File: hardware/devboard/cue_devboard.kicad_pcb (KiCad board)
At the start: 4 copper layers, 42 x 32 mm, 56 parts, among them J1 USB-C (power), J2 BATT, J3 LRA, J4 SWD, J5 EXP, SW1 USER, SW2 SHIP/WAKE, U1 BL54L15, U2 nPM1300, U3 LSM6DSV16BX, U4 T5838, U5 DRV2605L

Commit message: Dev board: fixes from the second layout review
- battery polarity marked (+/-) at J2; README: meter the cell's plug first
- LRA connector moved so the motor lines stay 2 mm from PDM_CLK, 5 mm from the mic hole
- nPM1300 exposed pad: 4 vias in the gaps between paste openings (no solder wicking)
- vias moved off the RT1, C6, C8 pads (via_off_pads.py); L1 joins C6 on top copper
- U3 pin 7 tied to ground (C8 shifted 0.4 mm, QVAR1 re-routed)
- silkscreen at JLCPCB minimums (1.0 mm text), TP net labels, button labels on top
- SW1/SW2 left out of BOM/CPL (hand-solder); fab/placement_check.png for the JLCPCB preview
DRC 0 violations, 0 unconnected; board = circuit pad for pad.

Co-Authored-By: Claude Opus 5.5 <noreply@anthropic.com>
Claude-Session: https://claude.ai/code/session_01DUSU7jbUyc6QVB5XjyAbxC
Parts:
- moved J3 12.0 mm to (35.0, 28.8)
- moved E1 8.00 mm to (23.0, 29.0)
- moved SW1 3.72 mm to (28.0, 24.2)
- moved C8 0.40 mm to (23.6, 20.7)
- turned C6 to -90 degrees
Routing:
- net VBAT: track 67.9 -> 86.3 mm, vias 3 -> 5
- net CC1: track 30.2 -> 16.2 mm
- net MIC_1V8: track 54.4 -> 42.8 mm
- net PDM_CLK: track 29.8 -> 19.6 mm
- net LRA_P: track 21.8 -> 29.2 mm, vias 2 -> 0
- net PMIC_INT: track 32.1 -> 37.6 mm, vias 3 -> 1
- net TDM_WCLK: track 13.9 -> 18.6 mm
- net 3V0: track 44.1 -> 39.7 mm, vias 2 -> 3
- net VSYS: track 57.6 -> 62.0 mm
- net TOUCH_E: track 11.1 -> 7.22 mm
- net I2C_SCL: track 63.8 -> 67.1 mm, vias 3 -> 4
- net HAPTIC_EN: track 11.7 -> 9.08 mm
- net MIC_WAKE: track 8.53 -> 10.9 mm, vias 0 -> 2
- net GND: track 48.5 -> 46.3 mm, vias 164 -> 159
- net MIC_THSEL: track 17.3 -> 15.3 mm
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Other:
- board text added: "+"
- board text added: "-"
- board text added: "1V8"
- board text added: "3V0"
- board text added: "BATT"
- board text added: "GND"
- board text added: "I2C_SCL"
- board text added: "I2C_SDA"
- board text added: "MIC"
- board text added: "PMIC_INT"
- board text added: "TOUCH"
- board text added: "VBAT"
- board text added: "VBUS"
- board text added: "VSYS"
- board text removed: "BATT+"

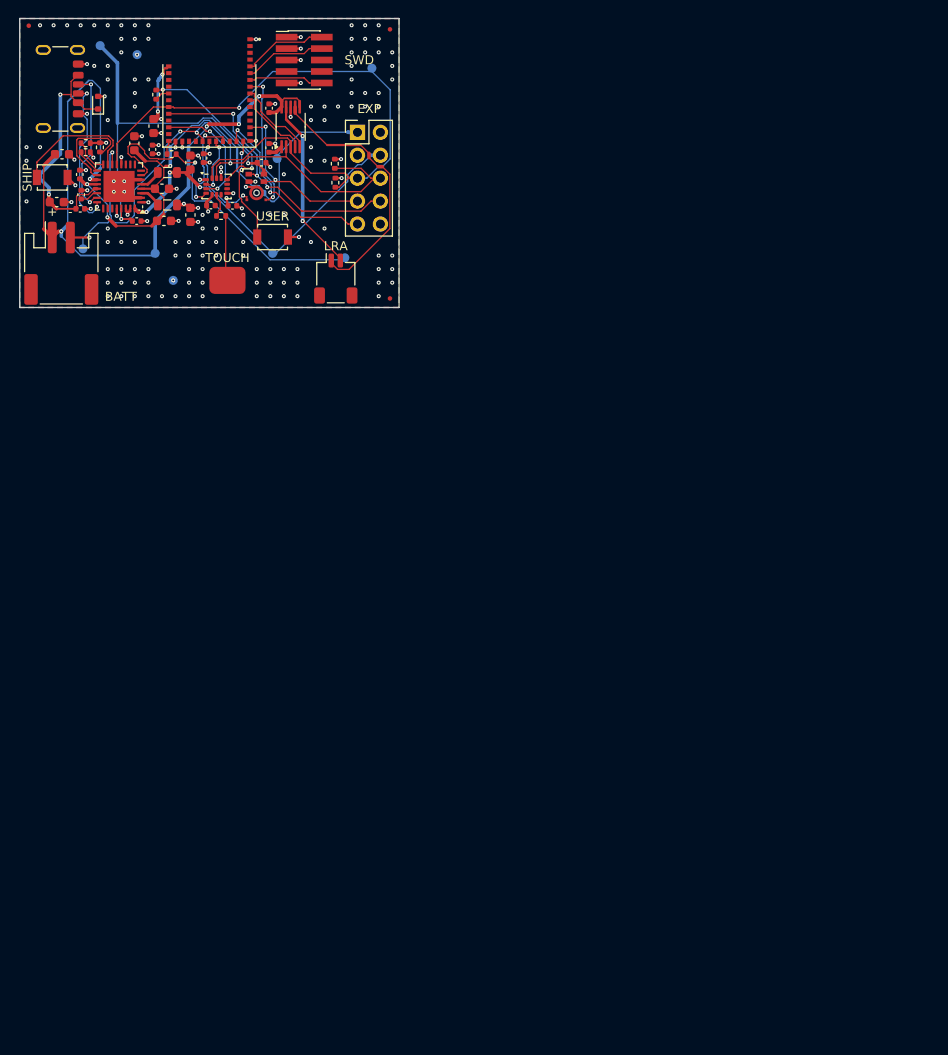
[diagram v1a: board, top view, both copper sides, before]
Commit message: Dev board: Big A's 33 x 21 mm re-layout (v4) plus review fixes
Big A: 35 x 20 mm class layout, J5 replaced by TP11-TP13, BUCK2 removed and
tied off per nPM1300 PS Config 2 (SW2 NC, VSET2 GND, VOUT2 VSYS), fiducials
removed, U3 pin 9 (QVAR2) to GND, USB shield pads on GND.

Review fixes: route U3 pin 9 to a new GND via (it was unconnected on the
board), delete 5 dangling stubs, drop J1's leftover S1 pin (shield is SH).
DRC: 0 unconnected, 0 parity issues; remaining items are courtyard, silk and
thermal-spoke warnings accepted by Big A. fab/bom.csv and cpl.csv are stale.

Co-Authored-By: Claude Opus 5.5 <noreply@anthropic.com>
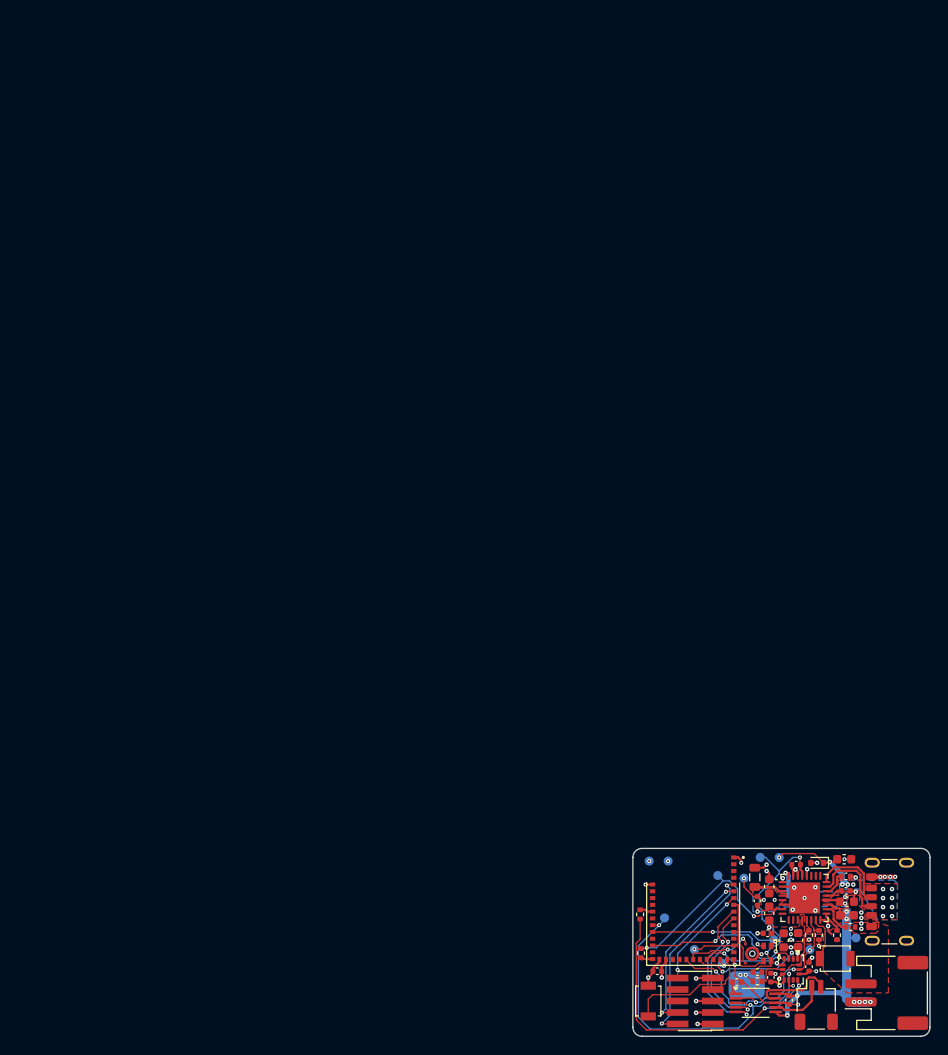
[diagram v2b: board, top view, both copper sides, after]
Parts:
- removed C7: 10uF, Capacitor_SMD:C_0603_1608Metric
- removed FID1, FID2, FID3: FID, Fiducial:Fiducial_0.5mm_Mask1mm
- removed J5: EXP, Connector_PinHeader_2.54mm:PinHeader_2x05_P2.54mm_Vertical
- removed L2: 2.2uH, Inductor_SMD:L_0805_2012Metric
- removed R4: 150k, Resistor_SMD:R_0402_1005Metric
- removed TP5: TP 3V0, TestPoint:TestPoint_Pad_D1.0mm
- added G***: LOGO, LOGO, B.Cu at (97.5, 109.2)
- added TP11: TestPoint, TestPoint:TestPoint_Pad_D1.0mm, B.Cu at (74.7, 103.1)
- added TP12: TestPoint, TestPoint:TestPoint_Pad_D1.0mm, B.Cu at (83.5, 102.0)
- added TP13: TestPoint, TestPoint:TestPoint_Pad_D1.0mm, B.Cu at (77.8, 104.6)
- E1: moved to B.Cu
- moved J1 130.1 mm to (97.4, 97.8), turned to 90 degrees
- moved SW2 122.5 mm to (90.3, 104.1)
- moved J2 122.0 mm to (96.0, 107.9), turned to 90 degrees
- moved C3 121.1 mm to (91.6, 99.3)
- moved R3 120.2 mm to (90.5, 101.5), turned to -90 degrees
- moved RT1 119.8 mm to (92.0, 100.6), turned to 0 degrees
- moved TP6 115.9 mm to (82.0, 92.9), turned to 180 degrees
- moved D1 115.9 mm to (88.3, 93.5), turned to 180 degrees
- moved C21 115.2 mm to (91.6, 97.8), turned to 0 degrees
- moved C11 114.3 mm to (85.2, 108.7), turned to -90 degrees
- moved C18 114.0 mm to (84.6, 102.1), turned to -90 degrees
- moved C2 113.6 mm to (91.3, 93.1)
- moved C1 113.6 mm to (91.5, 96.6)
- moved C17 113.5 mm to (91.5, 95.0), turned to 0 degrees
- moved J4 112.8 mm to (74.8, 108.8), turned to 180 degrees
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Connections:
- net 1V8 renamed /1V8
- net BTN_USER renamed /BTN_USER
- net CC1 renamed Net-(J1-CC1)
- net CC2 renamed Net-(J1-CC2)
- net HAPTIC_EN renamed /HAPTIC_EN
- net HAPTIC_TRIG renamed /HAPTIC_TRIG
- net I2C_SCL renamed /I2C_SCL
- net I2C_SDA renamed /I2C_SDA
- net IMU_INT1 renamed /IMU_INT1
- net LRA_N renamed /LRA_N
- net LRA_P renamed /LRA_P
- net MIC_1V8 renamed /MIC_1V8
- net MIC_THSEL renamed /MIC_THSEL
- net MIC_WAKE renamed /MIC_WAKE
- net NTC renamed Net-(U2-NTC)
- net PDM_CLK renamed /PDM_CLK
- net PDM_DIN renamed /PDM_DIN
- net PMIC_INT renamed /PMIC_INT
- net QVAR1 renamed Net-(U3-QVAR1)
- net SHPHLD renamed Net-(U2-SHPHLD)
- net SW1 renamed Net-(U2-SW1)
- net SWDCLK renamed /SWDCLK
- net SWDIO renamed /SWDIO
- net TDM_BCLK renamed /TDM_BCLK
- net TDM_DIN renamed /TDM_DIN
- net TDM_WCLK renamed /TDM_WCLK
- net TOUCH_E renamed Net-(E1-TOUCH_E)
- net U1_PMIC_INT renamed Net-(U1-P1.10)
- net U1_TDM_WCLK renamed Net-(U1-P1.11)
- net U5_REG renamed Net-(U5-REG)
- net VBAT renamed /VBAT
- net VBUS renamed /VBUS
- net VBUSOUT renamed Net-(U2-VBUSOUT)
- net VSET1 renamed Net-(U2-VSET1)
- net nRESET renamed /nRESET
- C20 pad 1: VSYS -> /VSYS
- C21 pad 1: VSYS -> /VSYS
- C4 pad 1: VSYS -> /VSYS
- C5 pad 1: VSYS -> /VSYS
- J2 pad MP: (no net) -> unconnected-(J2-NC-PadMP)_1
- J3 pad MP: (no net) -> unconnected-(J3-NC-PadMP)
- J4 pad 6: (no net) -> unconnected-(J4-NC-Pad6)
- J4 pad 7: (no net) -> unconnected-(J4-NC-Pad7)
- J4 pad 8: (no net) -> unconnected-(J4-NC-Pad8)
- TP3 pad 1: VSYS -> /VSYS
- U1 pad 11: (no net) -> unconnected-(U1-NC-Pad11)
- U1 pad 12: (no net) -> unconnected-(U1-NC-Pad12)
- U1 pad 13: (no net) -> unconnected-(U1-NC-Pad13)
- U1 pad 15: (no net) -> unconnected-(U1-NC-Pad15)
- U1 pad 18: EXP_P0_01 -> /EXP_P0_01
- U1 pad 19: (no net) -> unconnected-(U1-NC-Pad19)
- U1 pad 2: (no net) -> unconnected-(U1-NC-Pad2)
- U1 pad 24: (no net) -> unconnected-(U1-NC-Pad24)
- U1 pad 25: (no net) -> unconnected-(U1-NC-Pad25)
- U1 pad 29: (no net) -> unconnected-(U1-NC-Pad29)
- U1 pad 3: (no net) -> unconnected-(U1-NC-Pad3)
- U1 pad 31: (no net) -> unconnected-(U1-NC-Pad31)
- U1 pad 34: (no net) -> unconnected-(U1-NC-Pad34)
- U1 pad 36: (no net) -> unconnected-(U1-NC-Pad36)
- U1 pad 37: (no net) -> unconnected-(U1-NC-Pad37)
- U1 pad 38: (no net) -> unconnected-(U1-NC-Pad38)
- U1 pad 4: (no net) -> unconnected-(U1-NC-Pad4)
- U2 pad 10: (no net) -> unconnected-(U2-GPIO3-Pad10)
- U2 pad 11: (no net) -> unconnected-(U2-GPIO4-Pad11)
- U2 pad 16: VSET2 -> GND
- U2 pad 20: VSYS -> /VSYS
- U2 pad 25: (no net) -> unconnected-(U2-LED0-Pad25)
- U2 pad 26: (no net) -> unconnected-(U2-LED1-Pad26)
- U2 pad 27: (no net) -> unconnected-(U2-LED2-Pad27)
- U2 pad 32: 3V0 -> /VSYS
- U2 pad 4: VSYS -> /VSYS
- U2 pad 5: SW2 -> unconnected-(U2-SW2-Pad5)
- U2 pad 8: (no net) -> unconnected-(U2-GPIO1-Pad8)
- U2 pad 9: (no net) -> unconnected-(U2-GPIO2-Pad9)
- U3 pad 10: (no net) -> unconnected-(U3-NC-Pad10)
- U3 pad 9: (no net) -> GND
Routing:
- net VSYS: track 62.0 -> 0.00 mm, vias 3 -> 0
- net /VBAT: track 86.3 -> 33.0 mm, vias 5 -> 8
- net 3V0: track 39.7 -> 0.00 mm, vias 3 -> 0
- net /I2C_SCL: track 67.1 -> 28.2 mm
- net /I2C_SDA: track 72.8 -> 43.9 mm, vias 1 -> 3
- net /LRA_P: track 29.2 -> 6.10 mm
- net EXP_P0_01: track 20.9 -> 0.00 mm, vias 2 -> 0
- net /MIC_1V8: track 42.8 -> 23.9 mm
- net /PDM_DIN: track 31.9 -> 14.8 mm, vias 3 -> 2
- net /PMIC_INT: track 37.6 -> 22.3 mm, vias 1 -> 2
- net /VBUS: track 28.2 -> 13.0 mm, vias 2 -> 13
- net /TDM_WCLK: track 18.6 -> 32.6 mm
- net /SWDIO: track 9.46 -> 21.1 mm, vias 0 -> 2
- net GND: track 46.3 -> 57.3 mm, vias 159 -> 40
- net /LRA_N: track 19.5 -> 9.21 mm, vias 2 -> 0
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- added copper zone on F.Cu, net /1V8
- added copper zone on B.Cu, net /VBUS
- added copper zone on F.Cu, net /VBUS
- added copper zone on B.Cu, net /VSYS
- added copper zone on F.Cu, net /VSYS
- removed copper zone on B.Cu, net GND
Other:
- board size 42 x 32 mm -> 32.9 x 20.8 mm
- board text added: "MIC_1V8"
- board text added: "PDM_CLK"
- board text added: "PDM_DIN"
- board text added: "TMIC_INT"
- board text added: "shameless plug"
- board text removed: "+"
- board text removed: "-"
- board text removed: "2026-10"
- board text removed: "3V0"
- board text removed: "BATT"
- board text removed: "CUE rev A dev"
- board text removed: "LRA"
- board text removed: "MIC"
- board text removed: "PMIC_INT"
- board text removed: "SHIP"
- board text removed: "SWD"
- board text removed: "TOUCH"
- board text removed: "USER"

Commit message: Dev board: remove the via in the middle of U2's centre-pad paste opening; refill zones
The four corner vias stay. Zones refilled and saved. DRC: 0 unconnected,
0 parity issues, no copper clearance/short/hole errors; KiCad DRC at a 0.2 mm
test clearance shows nothing below the 0.127 mm rule.

Co-Authored-By: Claude Opus 5.5 <noreply@anthropic.com>
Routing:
- net GND: vias 40 -> 39
